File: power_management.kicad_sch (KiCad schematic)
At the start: 33 parts, among them J7 USB_C_Receptacle_PowerOnly_6P, J8 Conn_01x05_Pin, U2 BQ25895RTW, U3 TPS63900

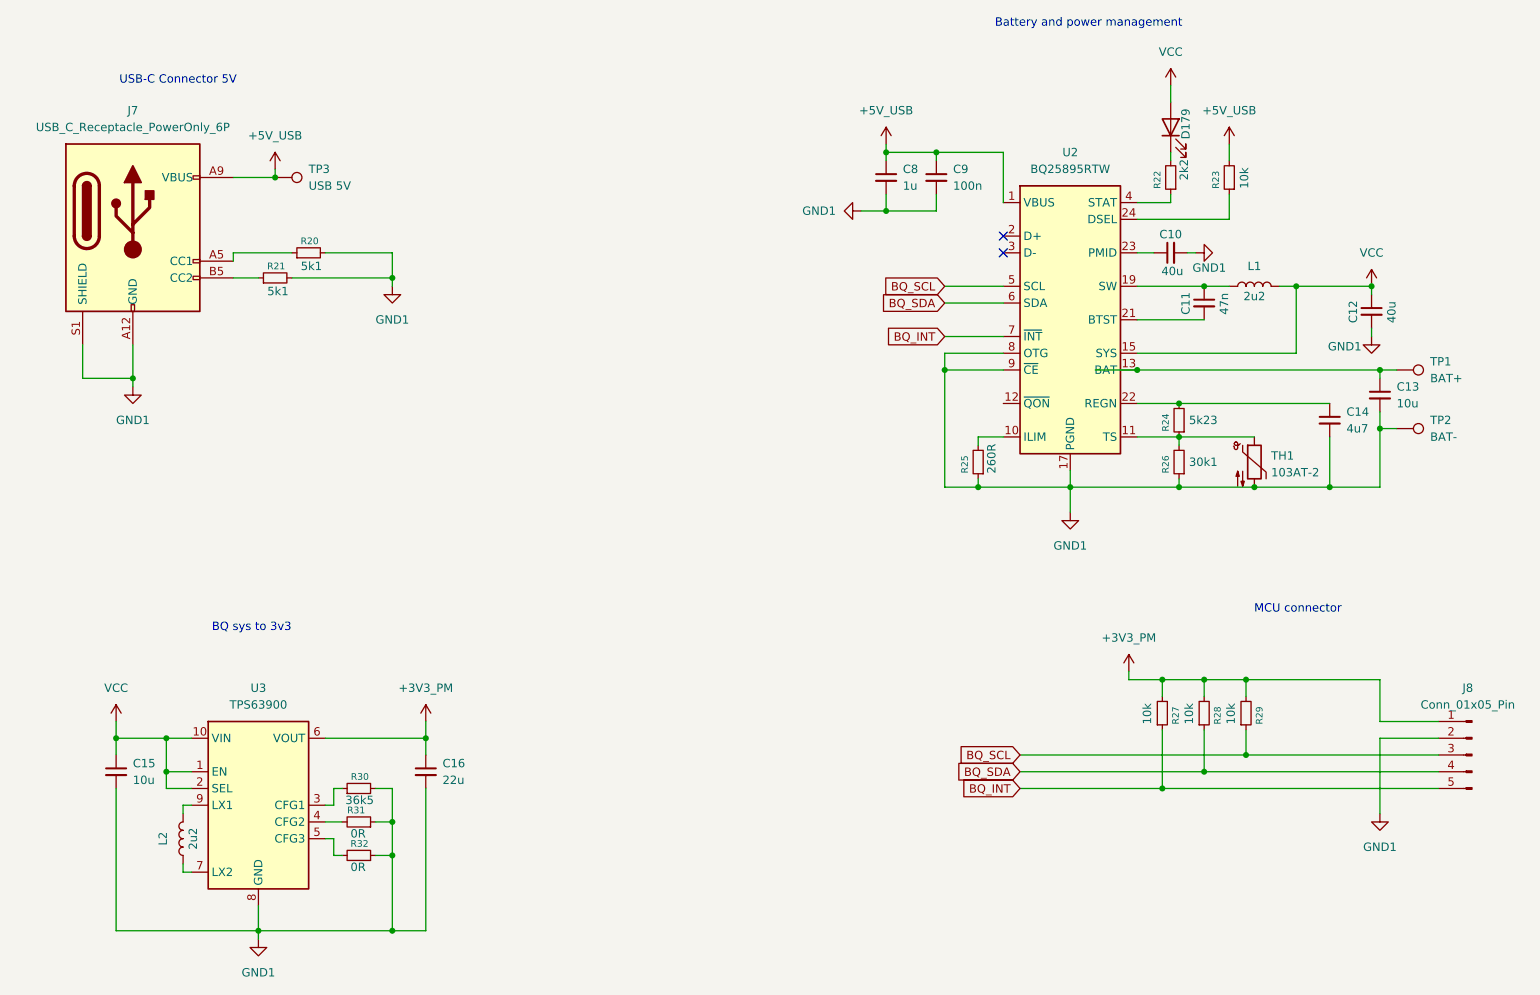
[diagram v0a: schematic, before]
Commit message: Change of concept - one board, not multiple
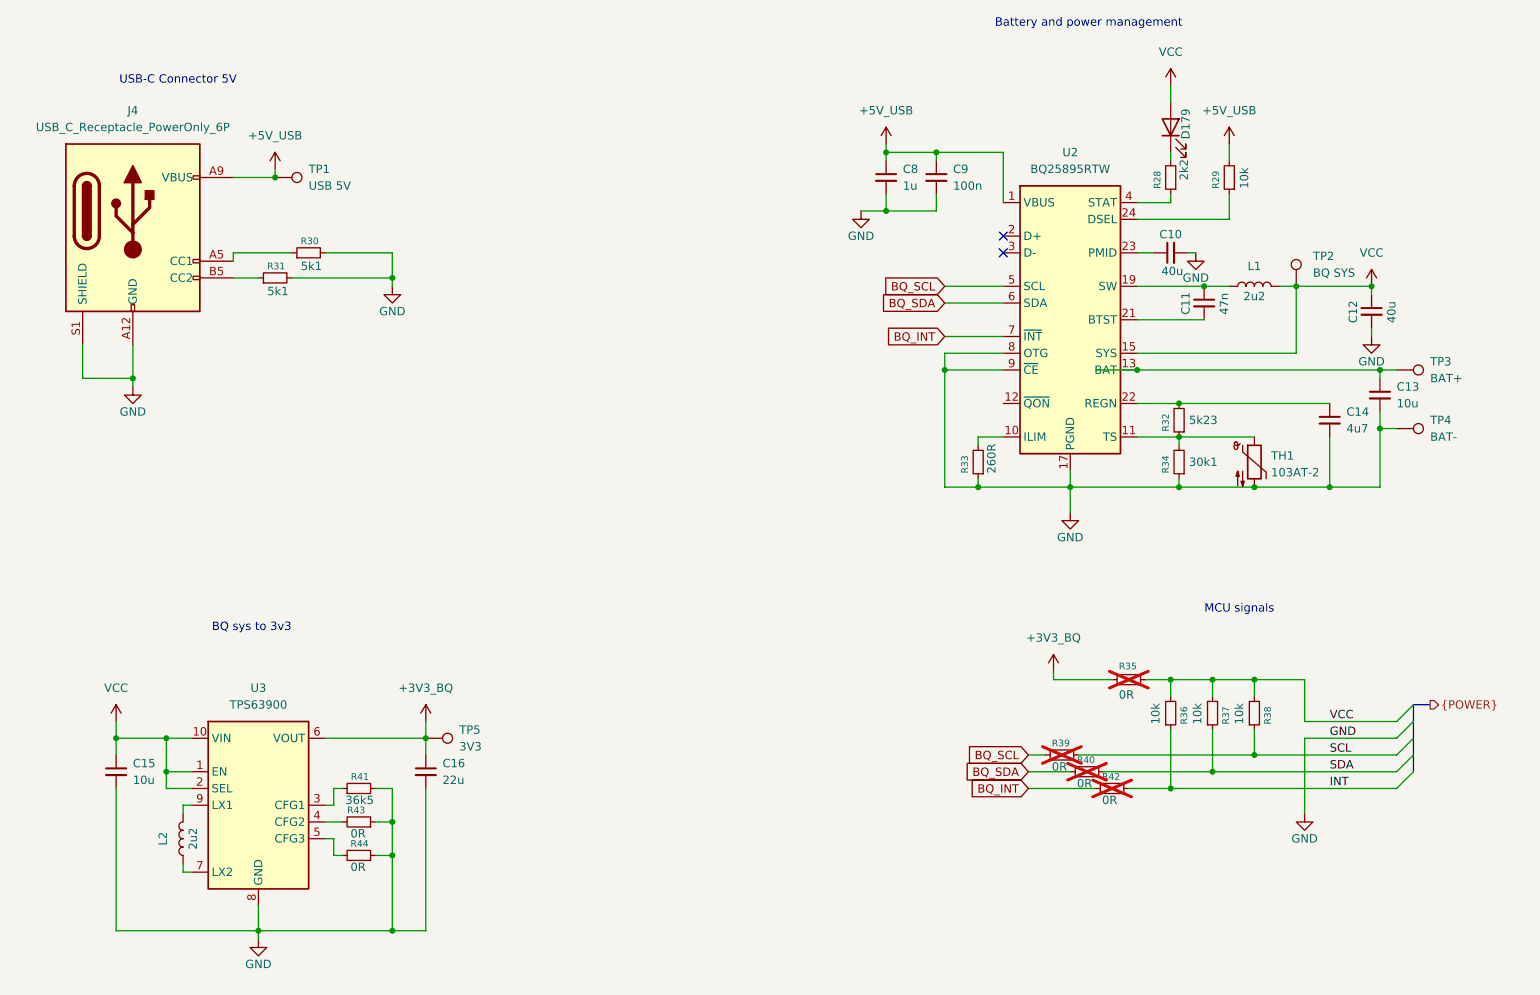
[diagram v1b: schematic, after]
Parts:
- removed J8: Conn_01x05_Pin, Connector_PinHeader_2.54mm:PinHeader_1x05_P2.54mm_Vertical, symbol Connector:Conn_01x05_Pin
- added R35, R39, R40, R42: 0R, Resistor_SMD:R_0603_1608Metric, symbol Device:R_Small
- added TP2: BQ SYS, TestPoint:TestPoint_Pad_D2.0mm, symbol Connector:TestPoint
- added TP5: 3V3, TestPoint:TestPoint_Pad_D2.0mm, symbol Connector:TestPoint
- renumbered J7 to J4, R22 to R28, R23 to R29, R20 to R30, R21 to R31, R24 to R32, R25 to R33, R26 to R34, R27 to R36, R28 to R37, R29 to R38, R30 to R41, R31 to R43, R32 to R44, TP3 to TP1, TP1 to TP3, TP2 to TP4
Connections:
- net BQ_INT: now also R42.2; no longer R36.1
- net BQ_SCL: now also R39.2; no longer R38.1
- net BQ_SDA: now also R40.2; no longer R37.1
- net VCC: now also R36.2, R37.2, R38.2, R35.1, TP2.1
- removed net +3V3_PM: C16.1, R36.2, R37.2, R38.2, U3.6 (VOUT)
- net GND1 renamed GND
- new net +3V3_BQ: C16.1, R35.2, TP5.1, U3.6 (VOUT)
- new net INT: R36.1, R42.1
- new net SCL: R38.1, R39.1
- new net SDA: R37.1, R40.1
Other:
- note added: "MCU signals"
- note removed: "MCU connector"
- moved on the sheet: R36, R37, R38

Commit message: Early pcb project
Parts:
- added TP4, TP7: GND, TestPoint:TestPoint_Pad_D2.0mm, symbol Connector:TestPoint
- J4: footprint (none) -> Connector_USB:USB_C_Receptacle_GCT_USB4135-GF-A_6P_TopMnt_Horizontal
- renumbered TP4 to TP5, TP5 to TP6
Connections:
- net GND: now also TP4.1, TP7.1
- no-connect marks 2 -> 3
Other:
- title: Title management -> Power management
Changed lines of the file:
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@@
 	(paper "A4")
 	(title_block
-		(title "Title management")
+		(title "Power management")
 		(date "2025-09-17")
 	)
@@
 	)
 	(junction
+		(at 92.71 170.18)
+		(diameter 0)
+		(color 0 0 0 0)
+	)
+	(junction
 		(at 226.06 132.08)
 		(diameter 0)
@@
 	)
 	(junction
-		(at 214.63 85.09)
-		(diameter 0)
-		(color 0 0 0 0)
-	)
-	(junction
 		(at 232.41 143.51)
 		(diameter 0)
@@
 		(at 194.31 67.31)
 	)
+	(no_connect
+		(at 194.31 90.17)
+	)
 	(bus_entry
 		(at 256.54 138.43)
@@
 	(wire
 		(pts
-			(xy 101.6 170.18) (xy 81.28 170.18)
+			(xy 101.6 170.18) (xy 92.71 170.18)
 		)
 		(stroke
@@
 	(wire
 		(pts
+			(xy 92.71 170.18) (xy 81.28 170.18)
+		)
+		(stroke
+			(width 0)
+			(type default)
+		)
+	)
+	(wire
+		(pts
 			(xy 214.63 62.23) (xy 228.6 62.23)
 		)
@@
 	(wire
 		(pts
-			(xy 208.28 85.09) (xy 214.63 85.09)
-		)
-		(stroke
-			(width 0)
-			(type default)
-		)
-	)
-	(wire
-		(pts
 			(xy 194.31 52.07) (xy 194.31 59.69)
 		)
@@
 			)
 		)
-		(property "Footprint" ""
+		(property "Footprint" "Connector_USB:USB_C_Receptacle_GCT_USB4135-GF-A_6P_TopMnt_Horizontal"
 			(at 66.04 60.96 0)
 			(effects
@@
 	)
 	(symbol
+		(lib_id "Connector:TestPoint")
+		(at 62.23 86.36 270)
+		(unit 1)
+		(exclude_from_sim no)
+		(in_bom yes)
+		(on_board yes)
+		(dnp no)
+		(fields_autoplaced yes)
+		(property "Reference" "TP4"
+			(at 67.31 85.0899 90)
+			(effects
+				(font
+					(size 1.27 1.27)
+				)
+				(justify left)
+			)
+		)
+		(property "Value" "GND"
+			(at 67.31 87.6299 90)
+			(effects
+				(font
+					(size 1.27 1.27)
+				)
+				(justify left)
+			)
+		)
+		(property "Footprint" "TestPoint:TestPoint_Pad_D2.0mm"
+			(at 62.23 91.44 0)
+			(effects
+				(font
+					(size 1.27 1.27)
+				)
+				(hide yes)
+			)
+		)
+		(property "Datasheet" "~"
+			(at 62.23 91.44 0)
+			(effects
+				(font
+					(size 1.27 1.27)
+				)
+				(hide yes)
+			)
+		)
+		(property "Description" "test point"
+			(at 62.23 86.36 0)
+			(effects
+				(font
+					(size 1.27 1.27)
+				)
+				(hide yes)
+			)
+		)
+		(pin "1"
+		)
+		(instances
+			(project "Eval_boards"
+				(path "/d7ecb1f3-4916-4ecb-8c6e-b89f175440e1/2d18b93a-1164-4a37-b4a8-6b00efa1e253"
+					(reference "TP4")
+					(unit 1)
+				)
+			)
+		)
+	)
+	(symbol
 		(lib_id "Device:R_Small")
 		(at 207.01 146.05 270)
@@
 		(on_board yes)
 		(dnp no)
-		(property "Reference" "TP4"
+		(property "Reference" "TP5"
 			(at 259.08 92.7099 90)
 			(effects
@@
 			(project "Eval_boards"
 				(path "/d7ecb1f3-4916-4ecb-8c6e-b89f175440e1/2d18b93a-1164-4a37-b4a8-6b00efa1e253"
-					(reference "TP4")
+					(reference "TP5")
 					(unit 1)
 				)
@@
 		(dnp no)
 		(fields_autoplaced yes)
-		(property "Reference" "TP5"
+		(property "Reference" "TP6"
 			(at 111.76 139.6999 90)
 			(effects
@@
 			(project "Eval_boards"
 				(path "/d7ecb1f3-4916-4ecb-8c6e-b89f175440e1/2d18b93a-1164-4a37-b4a8-6b00efa1e253"
-					(reference "TP5")
+					(reference "TP6")
 					(unit 1)
 				)
@@
 					(unit 1)
 				)
+			)
+		)
+	)
+	(symbol
+		(lib_id "Connector:TestPoint")
+		(at 92.71 170.18 180)
+		(unit 1)
+		(exclude_from_sim no)
+		(in_bom yes)
+		(on_board yes)
+		(dnp no)
+		(fields_autoplaced yes)
+		(property "Reference" "TP7"
+			(at 95.25 172.2119 0)
+			(effects
+				(font
+					(size 1.27 1.27)
+				)
+				(justify right)
+			)
+		)
+		(property "Value" "GND"
+			(at 95.25 174.7519 0)
+			(effects
+				(font
+					(size 1.27 1.27)
+				)
+				(justify right)
+			)
+		)
+		(property "Footprint" "TestPoint:TestPoint_Pad_D2.0mm"
+			(at 87.63 170.18 0)
+			(effects
+				(font
+					(size 1.27 1.27)
+				)
+				(hide yes)
+			)
+		)
+		(property "Datasheet" "~"
+			(at 87.63 170.18 0)
+			(effects
+				(font
+					(size 1.27 1.27)
+				)
+				(hide yes)
+			)
+		)
+		(property "Description" "test point"
+			(at 92.71 170.18 0)
+			(effects
+				(font
+					(size 1.27 1.27)
+				)
+				(hide yes)
+			)
+		)
+		(pin "1"
+		)
+		(instances
+			(project "Eval_boards"
+				(path "/d7ecb1f3-4916-4ecb-8c6e-b89f175440e1/2d18b93a-1164-4a37-b4a8-6b00efa1e253"
+					(reference "TP7")
+					(unit 1)
+				)

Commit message: Finished pcb project
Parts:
- removed R35, R39, R40, R42: 0R, Resistor_SMD:R_0603_1608Metric, symbol Device:R_Small
- removed TH1: 103AT-2, OptoDevice:R_LDR_4.9x4.2mm_P2.54mm_Vertical, symbol Device:Thermistor_NTC
- added JP10, JP7, JP8, JP9: SolderJumper_2_Open, Jumper:SolderJumper-2_P1.3mm_Open_TrianglePad1.0x1.5mm, symbol Jumper:SolderJumper_2_Open
- added R33: 10k, Resistor_SMD:R_0603_1608Metric, symbol Device:R_Small
- renumbered C8 to C10, C9 to C11, C10 to C12, C11 to C13, C12 to C15, C13 to C16, C15 to C8, C16 to C9, J4 to J3, L2 to L1, L1 to L2, R31 to R21, R30 to R22, R41 to R23, R43 to R24, R44 to R25, R33 to R26, R28 to R27, R36 to R28, R32 to R29, R34 to R30, R37 to R31, R29 to R32, R38 to R34, TP4 to TP1, TP1 to TP2, TP7 to TP3, TP6 to TP4, TP2 to TP5, TP3 to TP6, TP5 to TP7, U3 to U2, U2 to U3
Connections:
- net +3V3_BQ: now also JP9.1 (A)
- net BQ_INT: now also JP10.1 (A)
- net BQ_SCL: now also JP7.1 (A)
- net BQ_SDA: now also JP8.1 (A)
- net GND: now also R33.1
- net INT: now also JP10.2 (B)
- net VCC: no longer C15.1, C8.1, L2.2, R28.2, R31.2, R34.2, TP5.1, U2.1 (EN), U2.10 (VIN), U2.2 (SEL), U3.15 (SYS), U3.16 (SYS)
- net at R29.1, R30.2, U3.11 (TS): now also R33.2
- net +5V_USB renamed +5V
- net +5V: no longer R32.2
- net SCL renamed SCL_BQ
- net SCL_BQ: now also JP7.2 (B)
- net SDA renamed SDA_BQ
- net SDA_BQ: now also JP8.2 (B)
- new net +4V: C15.1, C8.1, L2.2, R32.2, TP5.1, U2.1 (EN), U2.10 (VIN), U2.2 (SEL), U3.15 (SYS), U3.16 (SYS)
- new net VCC_BQ: JP9.2 (B), R28.2, R31.2, R34.2

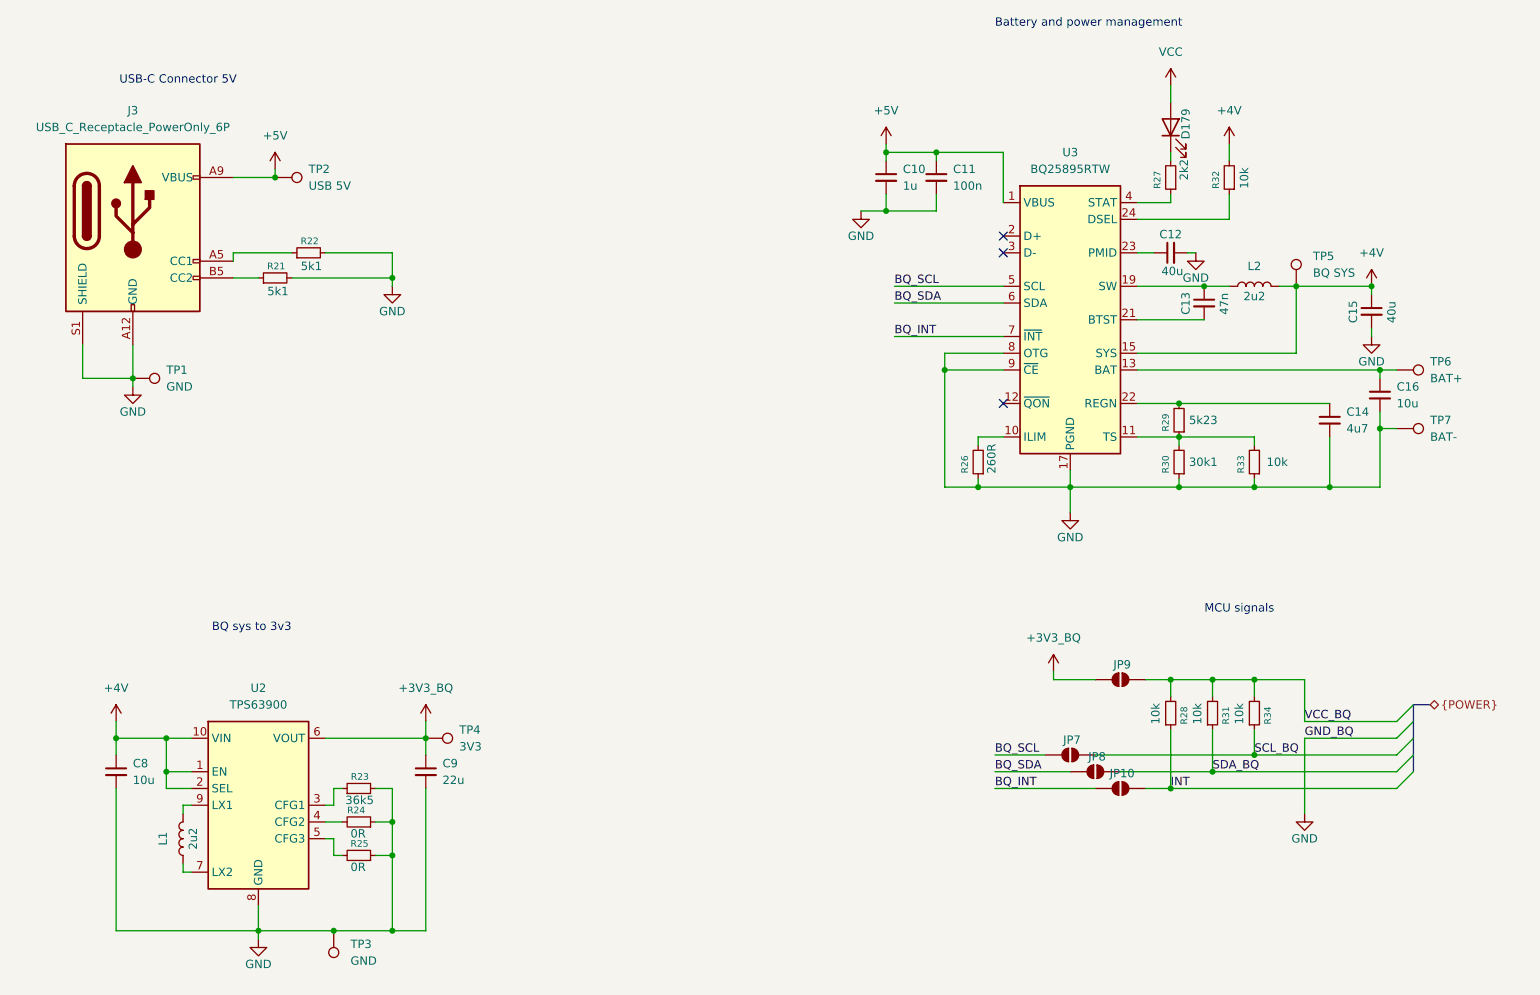
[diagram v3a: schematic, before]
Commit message: Add new mcu and better leds layout
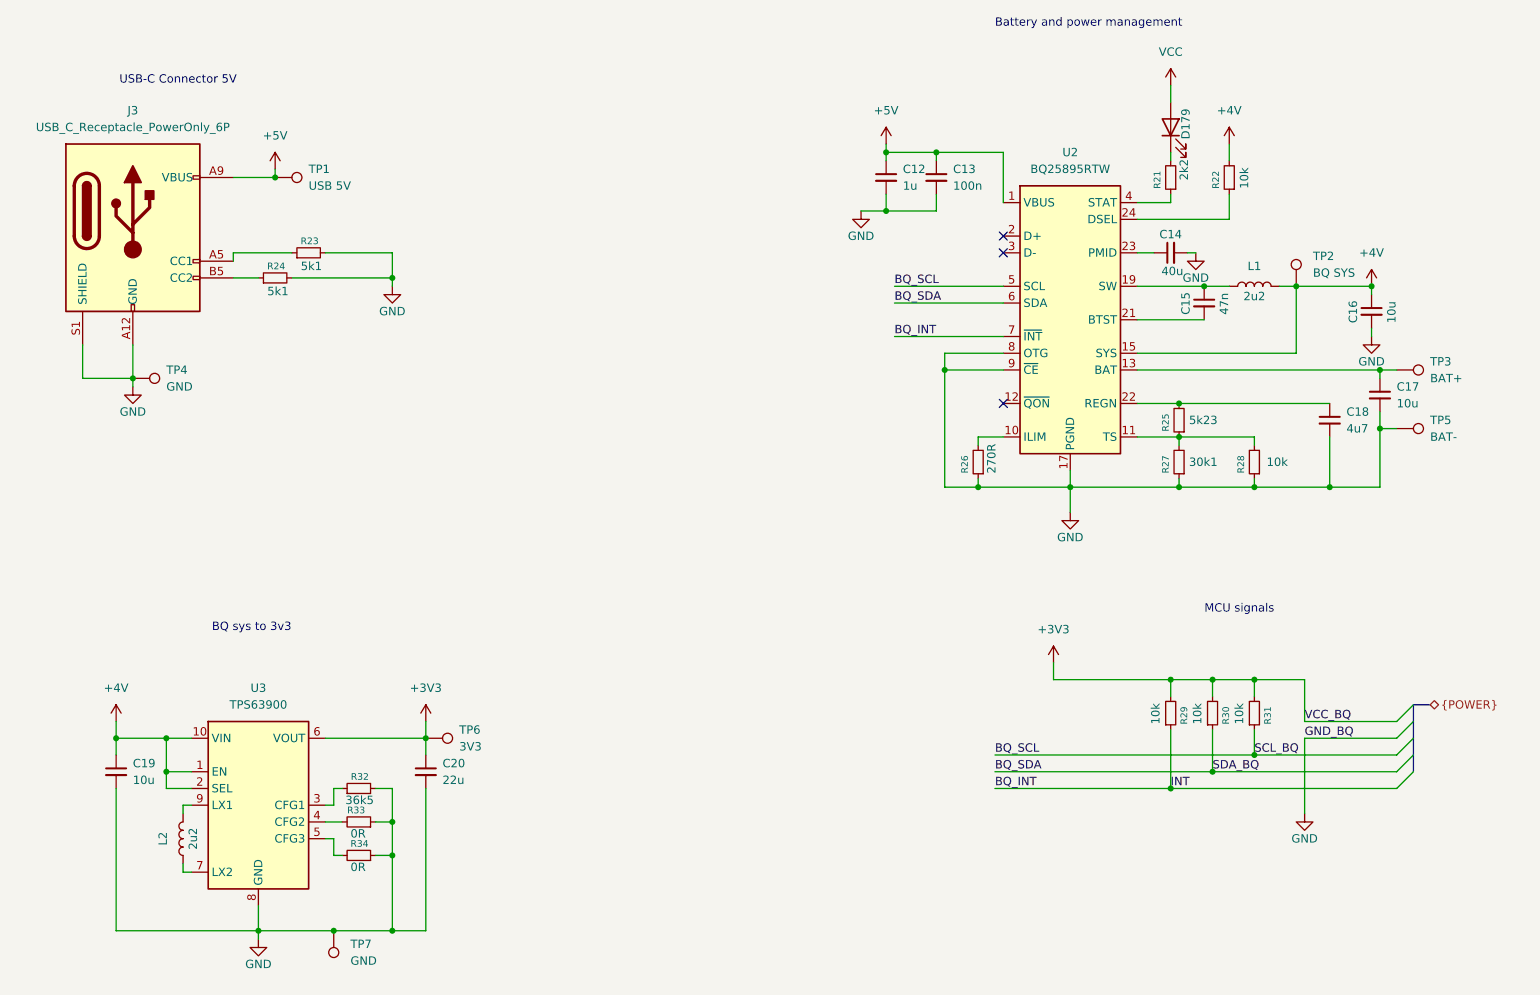
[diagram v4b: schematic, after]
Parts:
- removed JP10, JP7, JP8, JP9: SolderJumper_2_Open, Jumper:SolderJumper-2_P1.3mm_Open_TrianglePad1.0x1.5mm, symbol Jumper:SolderJumper_2_Open
- C16: renamed from C15; value 40u -> 10u
- R26: value 260R -> 270R
- TP1: renamed from TP2; footprint TestPoint:TestPoint_Pad_D2.0mm -> TestPoint:TestPoint_Pad_D1.0mm
- TP2: renamed from TP5; footprint TestPoint:TestPoint_Pad_D2.0mm -> TestPoint:TestPoint_Pad_D1.0mm
- TP4: renamed from TP1; footprint TestPoint:TestPoint_Pad_D2.0mm -> TestPoint:TestPoint_Pad_D1.0mm
- TP6: renamed from TP4; footprint TestPoint:TestPoint_Pad_D2.0mm -> TestPoint:TestPoint_Pad_D1.0mm
- TP7: renamed from TP3; footprint TestPoint:TestPoint_Pad_D2.0mm -> TestPoint:TestPoint_Pad_D1.0mm
- renumbered C10 to C12, C11 to C13, C12 to C14, C13 to C15, C16 to C17, C14 to C18, C8 to C19, C9 to C20, L2 to L1, L1 to L2, R27 to R21, R32 to R22, R22 to R23, R21 to R24, R29 to R25, R30 to R27, R33 to R28, R28 to R29, R31 to R30, R34 to R31, R23 to R32, R24 to R33, R25 to R34, TP6 to TP3, TP7 to TP5, U3 to U2, U2 to U3
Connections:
- net INT is gone; now on net BQ_INT: R29.1
- net SCL_BQ is gone; now on net BQ_SCL: R31.1
- net SDA_BQ is gone; now on net BQ_SDA: R30.1
- net VCC_BQ is gone; now on net +3V3: R29.2, R30.2, R31.2
- net +3V3_BQ renamed +3V3
